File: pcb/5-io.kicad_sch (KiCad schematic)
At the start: 0 parts

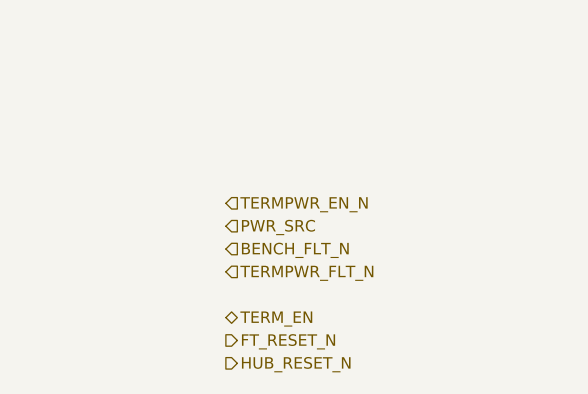
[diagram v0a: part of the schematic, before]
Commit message: Phase 3: populate power sheet; descriptive net names
Power sheet: bench eFuse (TPS259470A) with UVLO/OVLO string and EN
clamp, TPS2116 bench-priority mux with VBUS snubber, 3.3 V and 2.83 V
TPS73701 LDOs. Notes on the string's tap voltages, eFuse setting pins
and every DNP part. Project symbol library with the TPS259470A and
TPS73701DCQ drawn from the datasheet pin tables.

Nets renamed to spelled-out names (IS_BENCH_POWERED, *_INVERTED for
active-low, FEEDBACK, VTERMINATOR, TERMINATOR_EN) across the schematic,
pinout page, parts list and power block page.

Co-Authored-By: Claude Opus 5.5 <noreply@anthropic.com>
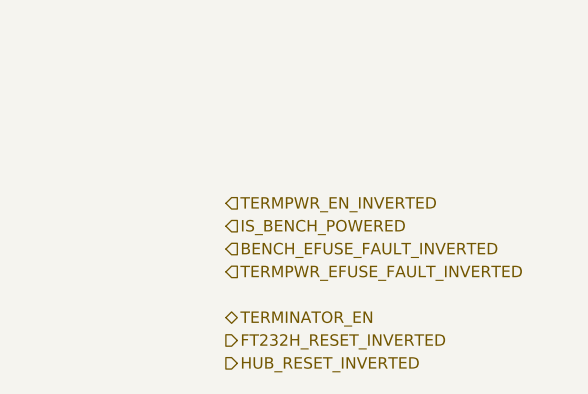
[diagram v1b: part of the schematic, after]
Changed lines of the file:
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@@
 	(hierarchical_label "SD_CMD" (shape bidirectional) (at 50.8 60.96 180) (effects (font (size 1.27 1.27)) (justify right)))
 	(hierarchical_label "SD_D0" (shape bidirectional) (at 50.8 63.5 180) (effects (font (size 1.27 1.27)) (justify right)))
-	(hierarchical_label "TERMPWR_EN_N" (shape input) (at 343.8 50.8 0) (effects (font (size 1.27 1.27)) (justify left)))
-	(hierarchical_label "PWR_SRC" (shape input) (at 343.8 53.34 0) (effects (font (size 1.27 1.27)) (justify left)))
-	(hierarchical_label "BENCH_FLT_N" (shape input) (at 343.8 55.88 0) (effects (font (size 1.27 1.27)) (justify left)))
-	(hierarchical_label "TERMPWR_FLT_N" (shape input) (at 343.8 58.42 0) (effects (font (size 1.27 1.27)) (justify left)))
-	(hierarchical_label "TERM_EN" (shape bidirectional) (at 343.8 63.5 0) (effects (font (size 1.27 1.27)) (justify left)))
-	(hierarchical_label "FT_RESET_N" (shape output) (at 343.8 66.04 0) (effects (font (size 1.27 1.27)) (justify left)))
-	(hierarchical_label "HUB_RESET_N" (shape output) (at 343.8 68.58 0) (effects (font (size 1.27 1.27)) (justify left)))
+	(hierarchical_label "TERMPWR_EN_INVERTED" (shape input) (at 343.8 50.8 0) (effects (font (size 1.27 1.27)) (justify left)))
+	(hierarchical_label "IS_BENCH_POWERED" (shape input) (at 343.8 53.34 0) (effects (font (size 1.27 1.27)) (justify left)))
+	(hierarchical_label "BENCH_EFUSE_FAULT_INVERTED" (shape input) (at 343.8 55.88 0) (effects (font (size 1.27 1.27)) (justify left)))
+	(hierarchical_label "TERMPWR_EFUSE_FAULT_INVERTED" (shape input) (at 343.8 58.42 0) (effects (font (size 1.27 1.27)) (justify left)))
+	(hierarchical_label "TERMINATOR_EN" (shape bidirectional) (at 343.8 63.5 0) (effects (font (size 1.27 1.27)) (justify left)))
+	(hierarchical_label "FT232H_RESET_INVERTED" (shape output) (at 343.8 66.04 0) (effects (font (size 1.27 1.27)) (justify left)))
+	(hierarchical_label "HUB_RESET_INVERTED" (shape output) (at 343.8 68.58 0) (effects (font (size 1.27 1.27)) (justify left)))
 	(embedded_fonts no)
 )
